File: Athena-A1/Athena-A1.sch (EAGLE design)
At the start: 80 parts, among them J1 MF-CON-MICROUSB-RIGHT, J2 TC2030-IDC-NL, J3 MF-CON-2.54mm-01x08, J4 MF-CON-2.54mm-01x08, J5 MF-CON-2.54mm-01x07, SW1 MF-SW-TACT-6MM, SW2 MF-SW-TACT-6MM, U1 PRTR5V0U2X,215, U2 MCP73831T-2ACI/OT, U3 AP2112K-3.3TRG1, U4 RT9080-18GJ5, U5 MK22FN128VLH10, U6 FE310, U7 32MBit, X1 JST 2-Pin, Y1 TSX-3225-16.0000MF18X-AC0, Y2 KX3211A0032.768000

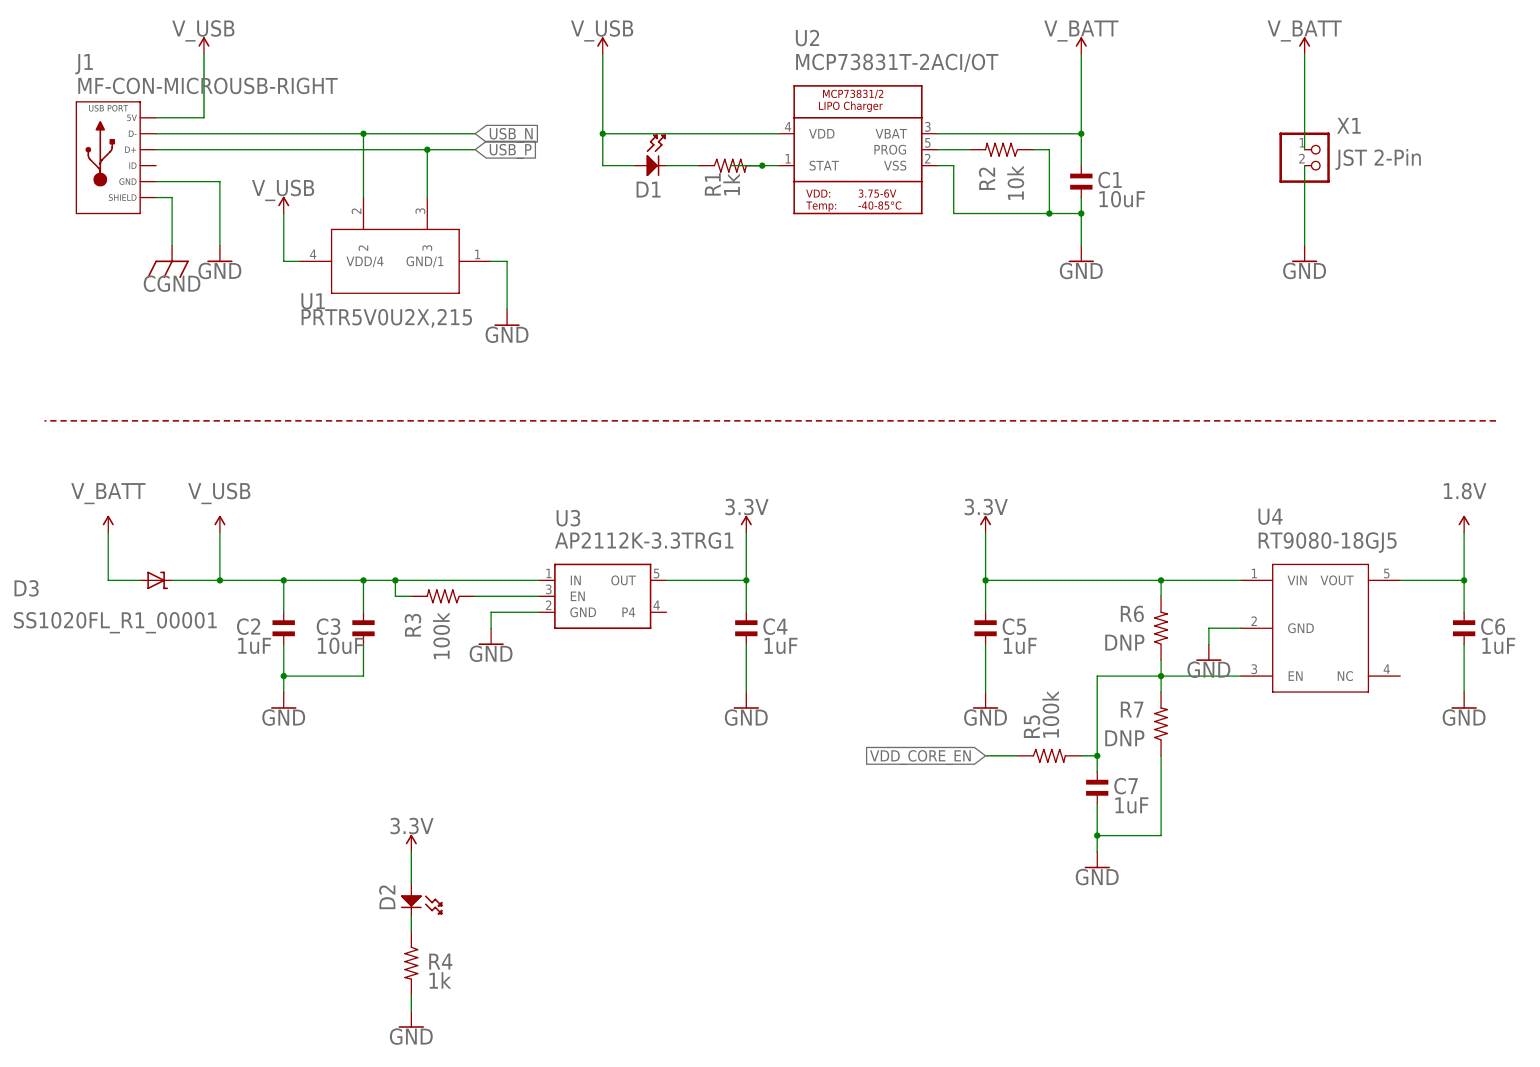
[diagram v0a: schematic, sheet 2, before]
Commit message: Updates post-review in progress
Sch: added power switch, improved symbols, added cap on Wake, added 0Ohm res to crystal, mikro gpio instead of wake/reset

Brd: moved tag connect to top, added clearance for mikro click brds, routed new switch, etc.

Todo: silkscreen cleanup and checking
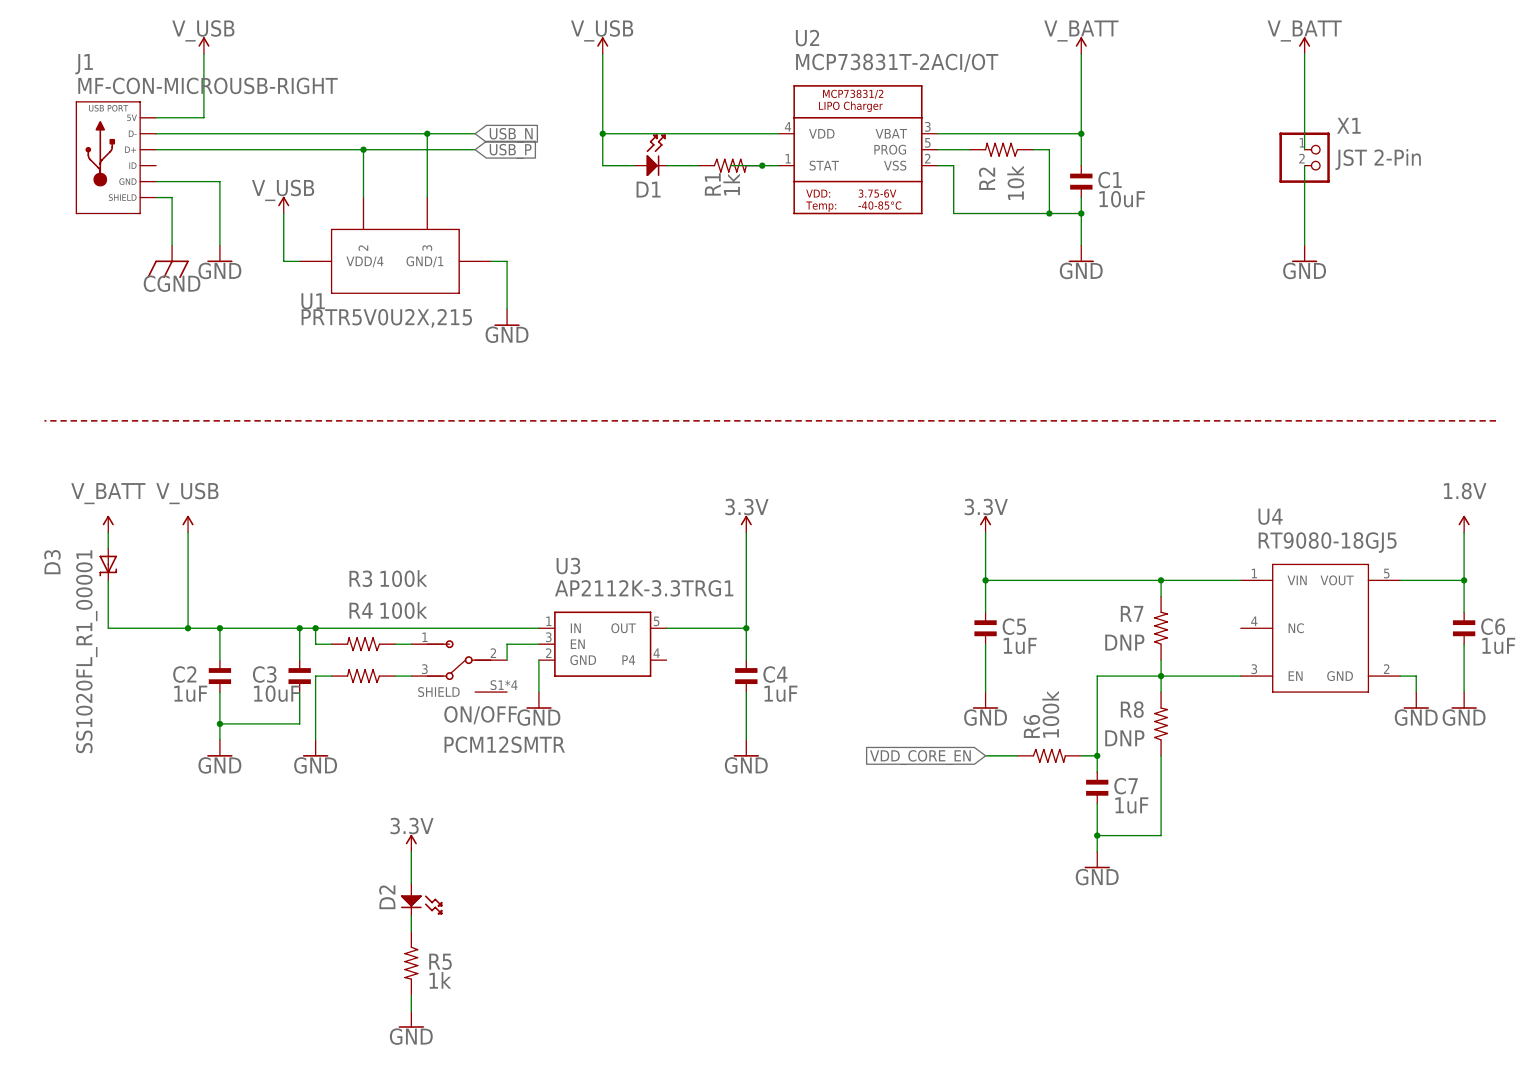
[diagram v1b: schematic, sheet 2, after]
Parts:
- removed B0, B1, B2, B3: TPB0,65, Athena-r1p0:TPB0,65
- added 0, 1, 2, 3: TPB0,65, Athena-A1:TPB0,65
- added C33: 0.1uF, Athena-A1:CAPACITOR_NP_0402
- added ON/OFF: PCM12SMTR, Athena-A1:PCM12SMTR
- added R21: 10, Athena-A1:RESISTOR_0402
- added R22, R23: 0, Athena-A1:RESISTOR_0402
- added X2: MIKROE_CLICKMINI, OSDZU3_ref_dsn:MIKROE_CLICKMINI
- C1, C10, C11, C12, C13, C14, C15, C16, C17, C18, C19, C2, C20, C21, C22, C23, C24, C25, C26, C27, C28, C3, C30, C31, C32, C4, C5, C6, C7, C8, C9: device Athena-r1p0:CAPACITOR_NP_0402 -> Athena-A1:CAPACITOR_NP_0402
- C29: value 0.1uF -> 0.01uF; device Athena-r1p0:CAPACITOR_NP_0402 -> Athena-A1:CAPACITOR_NP_0402
- D1: device Athena-r1p0:LED_SINGLE-0603-RED -> Athena-A1:LED_SINGLE-0603-RED
- D2: device Athena-r1p0:LED_SINGLE-0603-GREEN -> Athena-A1:LED_SINGLE-0603-GREEN
- D3: device Athena-r1p0:DIODE-SCHOTTKYSOD-123 -> Athena-A1:DIODE-SCHOTTKYSOD-123
- D4, D5: device Athena-r1p0:PESD0603-240TVS0603 -> Athena-A1:PESD0603-240TVS0603
- J1: device Athena-r1p0:USB_MICRO_RIGHT -> Athena-A1:USB_MICRO_RIGHT
- J2: device Athena-r1p0:TC2030-IDC-NL -> Athena-A1:TC2030-IDC-NL
- J3, J4: device Athena-r1p0:CON_01X08_PTH_2.54MM -> Athena-A1:CON_01X08_PTH_2.54MM
- J5: device Athena-r1p0:CON_01X07_PTH_2.54MM -> Athena-A1:CON_01X07_PTH_2.54MM
- MGT1, MGT2: device Athena-r1p0:MOUNTING_HOLE -> Athena-A1:MOUNTING_HOLE
- R1, R10, R11, R12, R14, R15, R18, R19, R2, R3, R7: device Athena-r1p0:RESISTOR_0402 -> Athena-A1:RESISTOR_0402
- R13: value 100k -> 100; device Athena-r1p0:RESISTOR_0402 -> Athena-A1:RESISTOR_0402
- R16: value 1M -> 100k; device Athena-r1p0:RESISTOR_0402 -> Athena-A1:RESISTOR_0402
- R17: value 100k -> 1M; device Athena-r1p0:RESISTOR_0402 -> Athena-A1:RESISTOR_0402
- R20: value 10 -> 100k; device Athena-r1p0:RESISTOR_0402 -> Athena-A1:RESISTOR_0402
- R4: value 1k -> 100k; device Athena-r1p0:RESISTOR_0402 -> Athena-A1:RESISTOR_0402
- R5: value 100k -> 1k; device Athena-r1p0:RESISTOR_0402 -> Athena-A1:RESISTOR_0402
- R6: value DNP -> 100k; device Athena-r1p0:RESISTOR_0402 -> Athena-A1:RESISTOR_0402
- R8: value 100k -> DNP; device Athena-r1p0:RESISTOR_0402 -> Athena-A1:RESISTOR_0402
- R9: value 100 -> 100k; device Athena-r1p0:RESISTOR_0402 -> Athena-A1:RESISTOR_0402
- SW1, SW2: device Athena-r1p0:TACT_4.2MM -> Athena-A1:TACT_4.2MM
- U1: device Athena-r1p0:PRTR5V0U2X,215 -> Athena-A1:PRTR5V0U2X,215
- U2: device Athena-r1p0:MCP73831/2 -> Athena-A1:MCP73831/2
- U3: device Athena-r1p0:AP2112 -> Athena-A1:AP2112
- U4: device Athena-r1p0:RT9080-18GJ5 -> Athena-A1:RT9080-18GJ5
- U5: device Athena-r1p0:MK22FN128VLH10 -> Athena-A1:MK22FN128VLH10
- U6: device Athena-r1p0:IC_MCU_SIFIVE_FE310 -> Athena-A1:IC_MCU_SIFIVE_FE310
- U7: device Athena-r1p0:IC_MEMORY_QSPI32MBIT -> Athena-A1:IC_MEMORY_QSPI32MBIT
- X1: device Athena-r1p0:CONNECTORS_BATT_JST_PH_2PIN -> Athena-A1:CONNECTORS_BATT_JST_PH_2PIN
- Y1: device Athena-r1p0:TSX-3225-16.0000MF18X-AC0 -> Athena-A1:TSX-3225-16.0000MF18X-AC0
- Y2: device Athena-r1p0:KX3211A0032.768000 -> Athena-A1:KX3211A0032.768000
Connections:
- removed net IO10: J5.PIN2, U6.IO10
- new net N$16: ON/OFF.2, U3.EN
- new net N$17: ON/OFF.3, R4.P$1
- new net N$18: C30.P$1, R17.P$1, R23.P$2, Y1.IN
- new net N$19: C31.P$1, R17.P$2, R22.P$1, Y1.OUT
- new net RST: J3.PIN2, U6.IO10
- net 1.8V: now also R13.P$1; no longer R12.P$1
- net 16MHZ_IN: now also R23.P$1; no longer C30.P$1, R16.P$1, Y1.IN
- net 16MHZ_OUT: now also R22.P$2; no longer C31.P$1, R16.P$2, Y1.OUT
- net 3.3V: now also C33.P$1, J5.PIN1, R16.P$1, R20.P$1, R7.P$2, R9.P$1; no longer C29.P$1, R13.P$1, R17.P$1, R6.P$2, R8.P$1
- net CGND: now also R21.P$1; no longer R20.P$1
- net DBG_RESET: now also R9.P$2; no longer R8.P$2
- net GND: now also C33.P$2, J5.PIN7, R21.P$2, R5.P$2, R8.P$1; no longer R20.P$2, R7.P$1
- net IO11: now also J5.PIN2; no longer J5.PIN3
- net IO19: now also J5.PIN3; no longer J5.PIN4
- net IO20: now also J5.PIN4; no longer J5.PIN5
- net IO21: now also J5.PIN5; no longer J5.PIN6
- net IO22: now also J5.PIN6; no longer J5.PIN7
- net IO9: now also J3.PIN1; no longer J5.PIN1
- net JTAG_TCK: now also R11.P$2; no longer R10.P$2
- net JTAG_TDI: now also R10.P$2; no longer R9.P$2
- net JTAG_TMS: now also R12.P$1; no longer R11.P$1
- net N$1: now also ON/OFF.1; no longer U3.EN
- net N$11: now also R10.P$1; no longer R9.P$1
- net N$12: now also 0.TP; no longer B0.TP
- net N$13: now also 1.TP; no longer B1.TP
- net N$14: now also 2.TP; no longer B2.TP
- net N$15: now also 3.TP; no longer B3.TP
- net N$2: now also R5.P$1; no longer R4.P$1
- net N$4: now also R6.P$2, R7.P$1, R8.P$2; no longer R5.P$2, R6.P$1, R7.P$2
- net N$8: now also R12.P$2; no longer R11.P$2
- net N$9: now also R11.P$1; no longer R10.P$1
- net PLL_AVDD: now also R13.P$2; no longer R12.P$2
- net QSPI_CS: now also R20.P$2; no longer R19.P$2
- net QSPI_DQ2: now also R18.P$2; no longer R17.P$2
- net QSPI_DQ3: now also R19.P$2; no longer R18.P$2
- net RESET: now also R16.P$2; no longer J3.PIN2, R14.P$2
- net USB_N: now also U1.3; no longer U1.2
- net USB_P: now also U1.2; no longer U1.3
- net VDD_CORE_EN: now also R6.P$1; no longer R5.P$1
- net WAKE: now also C29.P$1, R14.P$2; no longer J3.PIN1, R13.P$2
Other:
- note added: "16MHz TSX-3225 Crystal"
- note added: "ADD A COPYRIGHT AND LICENSE STATEMENT HERE"
- note added: "Dropout voltage of D3 will reduce operating range of batt. Replace w/auto-switching power mux in next rev. Maybe TPS2115A"
- note added: "July 12, 2022"
- note added: "Top-left pin of mikroBus std is an analog input. FE310 has no internal ADC, so this is GPIO instead. Recommend adding an I2C ADC chip (e.g. ADC121C027) in next rev."
- note removed: "16MHz TSX-3225 Oscillator"
- note removed: "June 6, 2022"
- moved on the sheet: C2, C3, C32, C4, D3, R10, R11, R13, R14, R17, R18, R19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

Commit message: Finished updates post-review
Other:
- note added: "Dropout voltage of D3 will reduce operating range of batt. Replace w/auto-switching power mux in next rev. See TPS2115A"
- note added: "July 25, 2022"
- note removed: "Dropout voltage of D3 will reduce operating range of batt. Replace w/auto-switching power mux in next rev. Maybe TPS2115A"
- note removed: "July 12, 2022"
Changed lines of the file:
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@@
 <setting verticaltext="up"/>
 </settings>
-<grid distance="100" unitdist="mil" unit="mil" style="lines" multiple="1" display="no" altdistance="0.01" altunitdist="inch" altunit="inch"/>
+<grid distance="0.1" unitdist="inch" unit="inch" style="lines" multiple="1" display="no" altdistance="0.01" altunitdist="inch" altunit="inch"/>
 <layers>
-<layer number="1" name="Top" color="4" fill="1" visible="yes" active="no"/>
-<layer number="2" name="Route2" color="16" fill="1" visible="yes" active="no"/>
-<layer number="3" name="Route3" color="17" fill="1" visible="yes" active="no"/>
-<layer number="4" name="Route4" color="18" fill="1" visible="yes" active="no"/>
-<layer number="5" name="Route5" color="19" fill="1" visible="yes" active="no"/>
-<layer number="6" name="Route6" color="25" fill="1" visible="yes" active="no"/>
-<layer number="7" name="Route7" color="26" fill="1" visible="yes" active="no"/>
-<layer number="8" name="Route8" color="27" fill="1" visible="yes" active="no"/>
-<layer number="9" name="Route9" color="28" fill="1" visible="yes" active="no"/>
-<layer number="10" name="Route10" color="29" fill="1" visible="yes" active="no"/>
-<layer number="11" name="Route11" color="30" fill="1" visible="yes" active="no"/>
-<layer number="12" name="Route12" color="20" fill="1" visible="yes" active="no"/>
-<layer number="13" name="Route13" color="21" fill="1" visible="yes" active="no"/>
-<layer number="14" name="Route14" color="22" fill="1" visible="yes" active="no"/>
-<layer number="15" name="Route15" color="23" fill="1" visible="yes" active="no"/>
-<layer number="16" name="Bottom" color="1" fill="1" visible="yes" active="no"/>
-<layer number="17" name="Pads" color="2" fill="1" visible="yes" active="no"/>
-<layer number="18" name="Vias" color="2" fill="1" visible="yes" active="no"/>
-<layer number="19" name="Unrouted" color="6" fill="1" visible="yes" active="no"/>
-<layer number="20" name="Dimension" color="24" fill="1" visible="yes" active="no"/>
-<layer number="21" name="tPlace" color="7" fill="1" visible="yes" active="no"/>
-<layer number="22" name="bPlace" color="7" fill="1" visible="yes" active="no"/>
-<layer number="23" name="tOrigins" color="15" fill="1" visible="yes" active="no"/>
-<layer number="24" name="bOrigins" color="15" fill="1" visible="yes" active="no"/>
-<layer number="25" name="tNames" color="7" fill="1" visible="yes" active="no"/>
-<layer number="26" name="bNames" color="7" fill="1" visible="yes" active="no"/>
-<layer number="27" name="tValues" color="7" fill="1" visible="yes" active="no"/>
-<layer number="28" name="bValues" color="7" fill="1" visible="yes" active="no"/>
+<layer number="1" name="Top" color="4" fill="1" visible="no" active="no"/>
+<layer number="2" name="Route2" color="16" fill="1" visible="no" active="no"/>
+<layer number="3" name="Route3" color="17" fill="1" visible="no" active="no"/>
+<layer number="4" name="Route4" color="18" fill="1" visible="no" active="no"/>
+<layer number="5" name="Route5" color="19" fill="1" visible="no" active="no"/>
+<layer number="6" name="Route6" color="25" fill="1" visible="no" active="no"/>
+<layer number="7" name="Route7" color="26" fill="1" visible="no" active="no"/>
+<layer number="8" name="Route8" color="27" fill="1" visible="no" active="no"/>
+<layer number="9" name="Route9" color="28" fill="1" visible="no" active="no"/>
+<layer number="10" name="Route10" color="29" fill="1" visible="no" active="no"/>
+<layer number="11" name="Route11" color="30" fill="1" visible="no" active="no"/>
+<layer number="12" name="Route12" color="20" fill="1" visible="no" active="no"/>
+<layer number="13" name="Route13" color="21" fill="1" visible="no" active="no"/>
+<layer number="14" name="Route14" color="22" fill="1" visible="no" active="no"/>
+<layer number="15" name="Route15" color="23" fill="1" visible="no" active="no"/>
+<layer number="16" name="Bottom" color="1" fill="1" visible="no" active="no"/>
+<layer number="17" name="Pads" color="2" fill="1" visible="no" active="no"/>
+<layer number="18" name="Vias" color="2" fill="1" visible="no" active="no"/>
+<layer number="19" name="Unrouted" color="6" fill="1" visible="no" active="no"/>
+<layer number="20" name="Dimension" color="24" fill="1" visible="no" active="no"/>
+<layer number="21" name="tPlace" color="7" fill="1" visible="no" active="no"/>
+<layer number="22" name="bPlace" color="7" fill="1" visible="no" active="no"/>
+<layer number="23" name="tOrigins" color="15" fill="1" visible="no" active="no"/>
+<layer number="24" name="bOrigins" color="15" fill="1" visible="no" active="no"/>
+<layer number="25" name="tNames" color="7" fill="1" visible="no" active="no"/>
+<layer number="26" name="bNames" color="7" fill="1" visible="no" active="no"/>
+<layer number="27" name="tValues" color="7" fill="1" visible="no" active="no"/>
+<layer number="28" name="bValues" color="7" fill="1" visible="no" active="no"/>
 <layer number="29" name="tStop" color="7" fill="3" visible="no" active="no"/>
 <layer number="30" name="bStop" color="7" fill="6" visible="no" active="no"/>
@@
 <layer number="35" name="tGlue" color="7" fill="4" visible="no" active="no"/>
 <layer number="36" name="bGlue" color="7" fill="5" visible="no" active="no"/>
-<layer number="37" name="tTest" color="7" fill="1" visible="yes" active="no"/>
-<layer number="38" name="bTest" color="7" fill="1" visible="yes" active="no"/>
+<layer number="37" name="tTest" color="7" fill="1" visible="no" active="no"/>
+<layer number="38" name="bTest" color="7" fill="1" visible="no" active="no"/>
 <layer number="39" name="tKeepout" color="4" fill="11" visible="no" active="no"/>
 <layer number="40" name="bKeepout" color="1" fill="11" visible="no" active="no"/>
@@
 <layer number="44" name="Drills" color="7" fill="1" visible="no" active="no"/>
 <layer number="45" name="Holes" color="7" fill="1" visible="no" active="no"/>
-<layer number="46" name="Milling" color="3" fill="1" visible="yes" active="no"/>
-<layer number="47" name="Measures" color="7" fill="1" visible="yes" active="no"/>
-<layer number="48" name="Document" color="7" fill="1" visible="yes" active="no"/>
-<layer number="49" name="Reference" color="7" fill="1" visible="yes" active="no"/>
-<layer number="50" name="ReferenceLS" color="7" fill="1" visible="yes" active="no"/>
-<layer number="51" name="tDocu" color="7" fill="1" visible="yes" active="no"/>
-<layer number="52" name="bDocu" color="7" fill="1" visible="yes" active="no"/>
-<layer number="53" name="tGND_GNDA" color="7" fill="1" visible="yes" active="no"/>
-<layer number="54" name="bGND_GNDA" color="7" fill="1" visible="yes" active="no"/>
-<layer number="56" name="wert" color="7" fill="1" visible="yes" active="no"/>
-<layer number="57" name="tCAD" color="7" fill="1" visible="yes" active="no"/>
-<layer number="59" name="tCarbon" color="7" fill="1" visible="yes" active="no"/>
-<layer number="60" name="bCarbon" color="7" fill="1" visible="yes" active="no"/>
+<layer number="46" name="Milling" color="3" fill="1" visible="no" active="no"/>
+<layer number="47" name="Measures" color="7" fill="1" visible="no" active="no"/>
+<layer number="48" name="Document" color="7" fill="1" visible="no" active="no"/>
+<layer number="49" name="Reference" color="7" fill="1" visible="no" active="no"/>
+<layer number="50" name="ReferenceLS" color="7" fill="1" visible="no" active="no"/>
+<layer number="51" name="tDocu" color="7" fill="1" visible="no" active="no"/>
+<layer number="52" name="bDocu" color="7" fill="1" visible="no" active="no"/>
+<layer number="53" name="tGND_GNDA" color="7" fill="1" visible="no" active="no"/>
+<layer number="54" name="bGND_GNDA" color="7" fill="1" visible="no" active="no"/>
+<layer number="56" name="wert" color="7" fill="1" visible="no" active="no"/>
+<layer number="57" name="tCAD" color="7" fill="1" visible="no" active="no"/>
+<layer number="59" name="tCarbon" color="7" fill="1" visible="no" active="no"/>
+<layer number="60" name="bCarbon" color="7" fill="1" visible="no" active="no"/>
 <layer number="88" name="SimResults" color="9" fill="1" visible="no" active="yes"/>
 <layer number="89" name="SimProbes" color="9" fill="1" visible="no" active="yes"/>
@@
 and research at Rice.  It is intended to be used in undergraduate lab courses and
 in VIP projects, therefore the design focus is on debug capability and I/O access.</text>
-<text x="114.3" y="91.44" size="2.54" layer="150" ratio="12">July 12, 2022</text>
+<text x="114.3" y="91.44" size="2.54" layer="150" ratio="12">July 25, 2022</text>
 <wire x1="0" y1="0" x2="0" y2="185.42" width="0.508" layer="94"/>
 <wire x1="248.92" y1="185.42" x2="248.92" y2="0" width="0.508" layer="94"/>
@@
 operating range of batt. Replace
 w/auto-switching power mux
-in next rev. Maybe TPS2115A</text>
+in next rev. See TPS2115A</text>
 </plain>
 <instances>
